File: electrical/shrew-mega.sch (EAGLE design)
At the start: 18 parts, among them IC1 Vreg +3V3, U1 DRV8231DSGR, U2 DRV8231DSGR, X1 PIN-1X-BIG, X2 PIN-1X-BIG, X3 PIN-1X-BIG, X4 PIN-1X-BIG, X5 PIN-1X-1.5MMSQ, X6 PIN-1X-1.5MMSQ

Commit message: rx mfg file trial run
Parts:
- added C10, C9: (no value), shrew-common:CAP0402-CAP
- added C8: (no value), shrew-common:CAP0805
- C6, C7: device shrew-common:CAP0402-CAP -> shrew-common:CAP0805
- IC1: value Vreg +3V3 -> (none); device shrew-common:V_REG_SOT89-SOT89 -> shrew-common:V_REG_LM1117SOT223
- U1, U2: value DRV8231DSGR -> DRV8244SQRYJRQ1; device shrew-core:DRV8231DSGR -> shrew-core:DRV8244SQRYJRQ1
- X5, X6: value PIN-1X-1.5MMSQ -> PIN-1X-BIG; device shrew-core:PIN-1X-1.5MMSQ -> shrew-core:PIN-1X-BIG
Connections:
- net +24V: now also C5.1, C6.1, C7.1
- net 3.3V: now also C8.1, IC1.OUT, IC1.OUT@1, U1.SLEEP_N, U2.SLEEP_N; no longer C5.1, IC1.VO, U1.VREF, U2.VREF
- net GND: now also C6.2, C7.2, C8.2, IC1.ADJ, U1.DIAG, U1.DRVOFF, U1.IPROPI, U1.ITRIP, U1.SR, U2.DIAG, U2.DRVOFF, U2.IPROPI, U2.ITRIP, U2.SR; no longer IC1.GND, IC1.TAB, U1.EPAD, U1.ISEN, U2.EPAD, U2.ISEN
- net N$10: now also C10.1, U2.OUT1, U2.OUT1_2; no longer C7.1, U1.OUT2
- net N$4: now also C9.2, U1.OUT2, U1.OUT2_2; no longer C6.2, U2.OUT1
- net N$5: now also C9.1, U1.OUT1, U1.OUT1_2; no longer C6.1, U2.OUT2
- net N$8: now also C10.2, U2.OUT2, U2.OUT2_2; no longer C7.2, U1.OUT1
- net SIG1: now also U2.EN_IN1; no longer U1.IN2
- net SIG2: now also U2.PH_IN2; no longer U1.IN1
- net SIG3: now also U1.EN_IN1; no longer U2.IN2
- net SIG4: now also U1.PH_IN2; no longer U2.IN1
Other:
- note added: "Current regulation disabled, OCP still used"
- note added: "Default slew rate 22V/us"
- note added: "Faults cause retry automatically"
- note added: "PWM mode"
- moved on the sheet: C1, C2, C3, C4, C5, C6, C7, JP1, R1

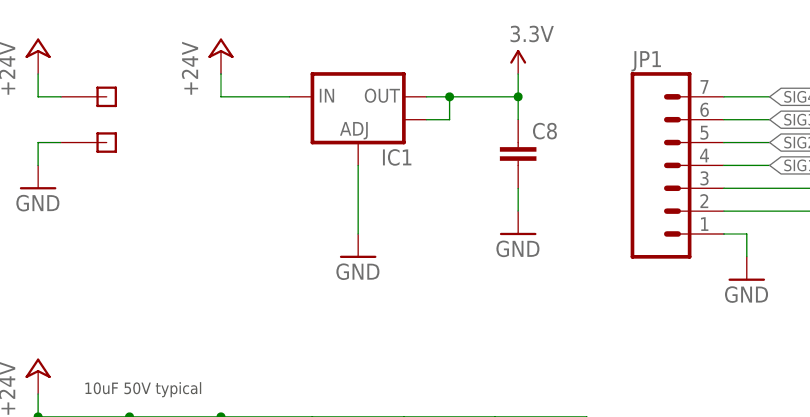
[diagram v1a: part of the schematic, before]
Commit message: changed v-reg on the mega variant to be more avail
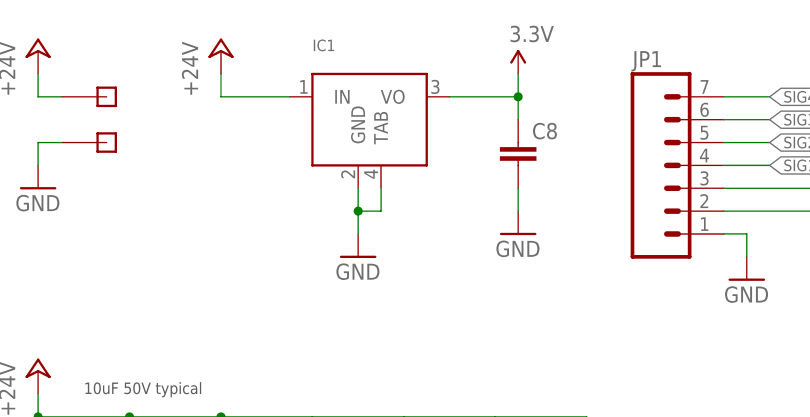
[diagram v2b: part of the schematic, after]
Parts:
- IC1: device shrew-common:V_REG_LM1117SOT223 -> shrew-common:V_REG_SOT-SOT223
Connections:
- net 3.3V: now also IC1.VO; no longer IC1.OUT, IC1.OUT@1
- net GND: now also IC1.GND, IC1.TAB; no longer IC1.ADJ

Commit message: schematic stitcher
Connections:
- net N$10 renamed MOTOR3
- net N$4 renamed MOTOR2
- net N$5 renamed MOTOR1
- net N$7 renamed V-ADC
- net N$8 renamed MOTOR4
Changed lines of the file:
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@@
 <wire x1="43.18" y1="58.42" x2="53.34" y2="58.42" width="0.1524" layer="91"/>
 <wire x1="53.34" y1="58.42" x2="53.34" y2="60.96" width="0.1524" layer="91"/>
+<junction x="43.18" y="58.42"/>
+<junction x="33.02" y="58.42"/>
+<junction x="22.86" y="58.42"/>
 </segment>
 <segment>
@@
 <wire x1="43.18" y1="71.12" x2="53.34" y2="71.12" width="0.1524" layer="91"/>
 <wire x1="53.34" y1="71.12" x2="53.34" y2="68.58" width="0.1524" layer="91"/>
+<junction x="22.86" y="71.12"/>
+<junction x="33.02" y="71.12"/>
+<junction x="43.18" y="71.12"/>
 </segment>
 <segment>
@@
 </segment>
 </net>
-<net name="N$4" class="0">
+<net name="MOTOR2" class="0">
 <segment>
 <pinref part="X1" gate="G$1" pin="P$1"/>
@@
 </segment>
 </net>
-<net name="N$5" class="0">
+<net name="MOTOR1" class="0">
 <segment>
 <pinref part="X2" gate="G$1" pin="P$1"/>
@@
 </segment>
 </net>
-<net name="N$8" class="0">
+<net name="MOTOR4" class="0">
 <segment>
 <pinref part="X3" gate="G$1" pin="P$1"/>
@@
 <pinref part="U2" gate="A" pin="OUT2"/>
 <wire x1="48.26" y1="-35.56" x2="50.8" y2="-35.56" width="0.1524" layer="91"/>
-</segment>
-</net>
-<net name="N$10" class="0">
+<junction x="50.8" y="-35.56"/>
+</segment>
+</net>
+<net name="MOTOR3" class="0">
 <segment>
 <pinref part="X4" gate="G$1" pin="P$1"/>
@@
 <wire x1="48.26" y1="-27.94" x2="50.8" y2="-27.94" width="0.1524" layer="91"/>
 <wire x1="50.8" y1="-27.94" x2="50.8" y2="-25.4" width="0.1524" layer="91"/>
+<junction x="50.8" y="-25.4"/>
 </segment>
 </net>
@@
 </segment>
 </net>
-<net name="N$7" class="0">
+<net name="V-ADC" class="0">
 <segment>
 <pinref part="JP1" gate="G$1" pin="3"/>

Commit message: initial work on integrated versions
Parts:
- added C11: (no value), shrew-common:CAP0805
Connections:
- new net SLEEP: U1.SLEEP_N, U2.SLEEP_N
- net +24V: now also C11.1
- net 3.3V: no longer U1.SLEEP_N, U2.SLEEP_N
- net GND: now also C11.2
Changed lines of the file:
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@@
 <layer number="97" name="Info" color="7" fill="1" visible="yes" active="yes"/>
 <layer number="98" name="Guide" color="6" fill="1" visible="yes" active="yes"/>
+<layer number="99" name="SpiceOrder" color="5" fill="1" visible="no" active="no"/>
 <layer number="100" name="Muster" color="7" fill="1" visible="no" active="no"/>
 <layer number="101" name="Patch_Top" color="12" fill="4" visible="no" active="yes"/>
@@
 <part name="P+11" library="shrew-common" deviceset="+24V" device=""/>
 <part name="P+12" library="shrew-common" deviceset="+24V" device=""/>
-<part name="P+13" library="shrew-common" deviceset="3.3V" device=""/>
 <part name="GND18" library="shrew-common" deviceset="GND" device=""/>
 <part name="X6" library="shrew-core" deviceset="PIN-1X" device="-BIG" value="PIN-1X-BIG"/>
@@
 <part name="JP1" library="shrew-common" deviceset="M07" device="-2MM-TH"/>
 <part name="GND1" library="shrew-common" deviceset="GND" device=""/>
-<part name="P+1" library="shrew-common" deviceset="3.3V" device=""/>
 <part name="R1" library="shrew-common" deviceset="RESISTOR" device="0402-RES"/>
 <part name="P+2" library="shrew-common" deviceset="+24V" device=""/>
@@
 <part name="P+3" library="shrew-common" deviceset="+24V" device=""/>
 <part name="P+4" library="shrew-common" deviceset="+24V" device=""/>
-<part name="P+5" library="shrew-common" deviceset="3.3V" device=""/>
-<part name="P+6" library="shrew-common" deviceset="3.3V" device=""/>
 <part name="GND4" library="shrew-common" deviceset="GND" device=""/>
 <part name="GND5" library="shrew-common" deviceset="GND" device=""/>
@@
 <part name="C7" library="shrew-common" deviceset="CAP" device="0805"/>
 <part name="IC1" library="shrew-common" deviceset="V_REG_SOT" device="-SOT223"/>
+<part name="P+1" library="shrew-common" deviceset="3.3V" device=""/>
+<part name="P+5" library="shrew-common" deviceset="3.3V" device=""/>
+<part name="C11" library="shrew-common" deviceset="CAP" device="0805"/>
+<part name="GND6" library="shrew-common" deviceset="GND" device=""/>
+<part name="P+6" library="shrew-common" deviceset="+24V" device=""/>
 </parts>
 <sheets>
@@
 <instance part="P+11" gate="1" x="-7.62" y="111.76"/>
 <instance part="P+12" gate="1" x="12.7" y="111.76"/>
-<instance part="P+13" gate="G$1" x="45.72" y="109.22"/>
 <instance part="GND18" gate="1" x="27.94" y="88.9"/>
 <instance part="X6" gate="G$1" x="0" y="101.6"/>
@@
 <instance part="JP1" gate="G$1" x="63.5" y="96.52"/>
 <instance part="GND1" gate="1" x="71.12" y="86.36"/>
-<instance part="P+1" gate="G$1" x="96.52" y="88.9"/>
 <instance part="R1" gate="G$1" x="86.36" y="96.52"/>
 <instance part="P+2" gate="1" x="104.14" y="104.14"/>
@@
 <instance part="P+3" gate="1" x="-5.08" y="38.1"/>
 <instance part="P+4" gate="1" x="-2.54" y="-20.32"/>
-<instance part="P+5" gate="G$1" x="-20.32" y="-35.56"/>
-<instance part="P+6" gate="G$1" x="-20.32" y="22.86"/>
 <instance part="GND4" gate="1" x="2.54" y="-66.04"/>
 <instance part="GND5" gate="1" x="2.54" y="-7.62"/>
@@
 <instance part="C7" gate="G$1" x="53.34" y="63.5"/>
 <instance part="IC1" gate="G$1" x="27.94" y="106.68"/>
+<instance part="P+1" gate="G$1" x="45.72" y="109.22"/>
+<instance part="P+5" gate="G$1" x="111.76" y="96.52"/>
+<instance part="C11" gate="G$1" x="81.28" y="68.58"/>
+<instance part="GND6" gate="1" x="81.28" y="60.96"/>
+<instance part="P+6" gate="1" x="81.28" y="78.74"/>
 </instances>
 <busses>
@@
 <label x="50.8" y="-48.26" size="1.27" layer="95" xref="yes"/>
 </segment>
-</net>
-<net name="3.3V" class="0">
-<segment>
-<pinref part="C8" gate="G$1" pin="1"/>
-<pinref part="P+13" gate="G$1" pin="3.3V"/>
-<wire x1="45.72" y1="109.22" x2="45.72" y2="106.68" width="0.1524" layer="91"/>
-<pinref part="IC1" gate="G$1" pin="VO"/>
-<wire x1="45.72" y1="106.68" x2="45.72" y2="104.14" width="0.1524" layer="91"/>
-<wire x1="38.1" y1="106.68" x2="45.72" y2="106.68" width="0.1524" layer="91"/>
-<junction x="45.72" y="106.68"/>
-</segment>
-<segment>
-<pinref part="JP1" gate="G$1" pin="2"/>
-<pinref part="P+1" gate="G$1" pin="3.3V"/>
-<wire x1="68.58" y1="93.98" x2="78.74" y2="93.98" width="0.1524" layer="91"/>
-<wire x1="78.74" y1="93.98" x2="78.74" y2="86.36" width="0.1524" layer="91"/>
-<wire x1="78.74" y1="86.36" x2="96.52" y2="86.36" width="0.1524" layer="91"/>
-<wire x1="96.52" y1="86.36" x2="96.52" y2="88.9" width="0.1524" layer="91"/>
-</segment>
+<segment>
+<pinref part="C11" gate="G$1" pin="2"/>
+<pinref part="GND6" gate="1" pin="GND"/>
+<wire x1="81.28" y1="66.04" x2="81.28" y2="63.5" width="0.1524" layer="91"/>
+</segment>
+</net>
+<net name="SLEEP" class="0">
 <segment>
 <pinref part="U1" gate="A" pin="SLEEP_N"/>
-<pinref part="P+6" gate="G$1" pin="3.3V"/>
-<wire x1="5.08" y1="20.32" x2="-20.32" y2="20.32" width="0.1524" layer="91"/>
-<wire x1="-20.32" y1="20.32" x2="-20.32" y2="22.86" width="0.1524" layer="91"/>
+<wire x1="5.08" y1="20.32" x2="2.54" y2="20.32" width="0.1524" layer="91"/>
+<label x="2.54" y="20.32" size="1.27" layer="95" rot="R180" xref="yes"/>
 </segment>
 <segment>
 <pinref part="U2" gate="A" pin="SLEEP_N"/>
-<pinref part="P+5" gate="G$1" pin="3.3V"/>
-<wire x1="5.08" y1="-38.1" x2="-20.32" y2="-38.1" width="0.1524" layer="91"/>
-<wire x1="-20.32" y1="-38.1" x2="-20.32" y2="-35.56" width="0.1524" layer="91"/>
+<wire x1="5.08" y1="-38.1" x2="2.54" y2="-38.1" width="0.1524" layer="91"/>
+<label x="2.54" y="-38.1" size="1.27" layer="95" rot="R180" xref="yes"/>
 </segment>
 </net>
@@
 <wire x1="-5.08" y1="33.02" x2="-5.08" y2="35.56" width="0.1524" layer="91"/>
 </segment>
+<segment>
+<pinref part="C11" gate="G$1" pin="1"/>
+<pinref part="P+6" gate="1" pin="+24V"/>
+<wire x1="81.28" y1="73.66" x2="81.28" y2="76.2" width="0.1524" layer="91"/>
+</segment>
 </net>
 <net name="MOTOR2" class="0">
@@
 </segment>
 </net>
+<net name="3.3V" class="0">
+<segment>
+<pinref part="P+5" gate="G$1" pin="3.3V"/>
+<wire x1="111.76" y1="96.52" x2="111.76" y2="93.98" width="0.1524" layer="91"/>
+<pinref part="JP1" gate="G$1" pin="2"/>
+<wire x1="111.76" y1="93.98" x2="68.58" y2="93.98" width="0.1524" layer="91"/>
+</segment>
+<segment>
+<pinref part="IC1" gate="G$1" pin="VO"/>
+<pinref part="P+1" gate="G$1" pin="3.3V"/>
+<wire x1="38.1" y1="106.68" x2="45.72" y2="106.68" width="0.1524" layer="91"/>
+<wire x1="45.72" y1="106.68" x2="45.72" y2="109.22" width="0.1524" layer="91"/>
+<pinref part="C8" gate="G$1" pin="1"/>
+<wire x1="45.72" y1="104.14" x2="45.72" y2="106.68" width="0.1524" layer="91"/>
+<junction x="45.72" y="106.68"/>
+</segment>
+</net>

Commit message: up-rev
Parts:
- removed JP1: (no value), shrew-common:M07-2MM-TH
- added ANT1, ANT2: 74889302450, shrew-common:ANTENNA2SMD
- added C12: DNP, shrew-common:CAP0402-CAP
- added C13, C17: 470n, shrew-common:CAP0402-REV
- added C14, C15: (no value), shrew-common:CAP0402-CAP
- added C16, C18, C19, C20, C21, C22, C23: (no value), shrew-common:CAP0805
- added C24, C25, C27: 10u, shrew-common:CAP0805
- added C26: 100n, shrew-common:CAP0402-REV
- added D1: 3V6, shrew-common:DIODE-ZENER-BZT52
- added D2: (no value), shrew-common:DIODESOD
- added EDGE1: (no value), shrew-common:M05PTH
- added FL1: 2450FM07D0034T, shrew-core:2450FM07D0034T
- added L1: 15u, shrew-common:INDUCTOR0805
- added L2: 6u8, shrew-common:INDUCTOR0805
- added LED1: SK6812-EC20, shrew-core:SK6812-EC20
- added R2, R3: 10K, shrew-common:RESISTOR0402-REV
- added R4: (no value), shrew-common:RESISTOR0402-RES
- added U3, U4: DRV8244SQRYJRQ1, shrew-core:DRV8244SQRYJRQ1
- added Y1: 52MHz TCXO, shrew-common:OSCILLATOR-TG2016SMN
- C1: value (none) -> 1n; device shrew-common:CAP0805 -> shrew-common:CAP0402-REV
- C10, C9: value (none) -> 100n; device shrew-common:CAP0402-CAP -> shrew-common:CAP0402-REV
- C11: value (none) -> 10uF 25V
- C2: value (none) -> 470n; device shrew-common:CAP0805 -> shrew-common:CAP0402-REV
- C3, C4: value (none) -> 10n; device shrew-common:CAP0805 -> shrew-common:CAP0402-REV
- C5, C6, C7, C8: value (none) -> 100n; device shrew-common:CAP0805 -> shrew-common:CAP0402-REV
- IC1: value (none) -> LMR16006YQ3DDCTQ1; device shrew-common:V_REG_SOT-SOT223 -> shrew-core:LMR16006XDDCR
- R1: value (none) -> 10K; device shrew-common:RESISTOR0402-RES -> shrew-common:RESISTOR0402-REV
- U1: value DRV8244SQRYJRQ1 -> ESP32-PICO-D4; device shrew-core:DRV8244SQRYJRQ1 -> shrew-core:ESP32-PICO-D4
- U2: value DRV8244SQRYJRQ1 -> SX1280IMLTRT; device shrew-core:DRV8244SQRYJRQ1 -> shrew-core:SX1280IMLTRT
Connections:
- removed net SLEEP: U1.SLEEP_N, U2.SLEEP_N
- new net AUX1: EDGE1.1, U1.IO19
- new net AUX2: EDGE1.2, U1.IO22
- new net BATT-ADC: C17.1, D1.C, R2.2, R3.1, U1.IO4
- new net ESP-BOOT: C12.2, U1.IO0(BOOT)
- new net ESP-EN: C13.2, R1.1, U1.EN
- new net N$1: ANT1.SIGNAL, U1.LNA_IN
- new net N$10: C26.1, D2.C, IC1.SW, L2.1
- new net N$11: C3.2, U2.VR_PA
- new net N$2: C1.1, Y1.OUT
- new net N$3: C1.2, U2.XTA
- new net N$4: C26.2, IC1.CB
- new net N$5: U1.IO14
- new net N$6: FL1.IN, U2.RFIO
- new net N$7: ANT2.SIGNAL, FL1.OUT
- new net N$8: U1.IO2
- new net N$9: L1.2, U2.DCC_SW
- new net RADIO-BUSY: U1.IO23, U2.BUSY
- new net RADIO-CS: U1.IO32, U2.NSS_CTS
- new net RADIO-DIO: U1.IO18, U2.DIO1
- new net RADIO-RST: U1.IO21, U2.NRESET, U3.SLEEP_N, U4.SLEEP_N
- new net RADIO-VDD: C2.2, C4.2, L1.1, U2.DCC_FB, U2.VDD_INN
- new net RGBLED: LED1.DIN, U1.IO5
- new net SPI-MISO: U1.IO26, U2.MISO_TX
- new net SPI-MOSI: U1.IO25, U2.MOSI_RX
- new net SPI-SCK: U1.IO33, U2.SCK_RTSN
- new net U0RXD: EDGE1.3, U1.U0RXD(IO3)
- new net U0TXD: EDGE1.4, U1.U0TXD(IO1)
- net +24V: now also C16.1, C18.1, C19.1, C20.1, C21.1, C22.1, C23.1, C24.1, IC1.SHDN, IC1.VIN, R4.2, U3.VM, U4.VM; no longer C1.1, C11.1, C2.1, C3.1, C4.1, C5.1, C6.1, C7.1, IC1.IN, R1.2, U1.VM, U2.VM
- net 3.3V: now also C10.1, C11.1, C25.1, C27.1, C5.2, C6.2, C7.2, C9.1, IC1.FB, L2.2, LED1.VDD, R1.2, U1.VDD3P3_CPU, U1.VDD3P3_RTC, U1.VDDA, U1.VDDA3P3, U1.VDD_SDIO, U2.VBAT, U2.VBAT_IO, Y1.VCC; no longer IC1.VO, JP1.2
- net GND: now also C10.2, C12.1, C13.1, C16.2, C17.2, C18.2, C19.2, C2.1, C20.2, C21.2, C22.2, C23.2, C24.2, C25.2, C27.2, C3.1, C4.1, C5.1, C6.1, C7.1, C9.2, D1.A, D2.A, EDGE1.5, LED1.VSS(GND), R2.1, U1.IO15/MTDO, U2.GND_2, U2.GND_3, U2.GND_4, U2.GND_5, U2.GND_6, U2.GND_7, U3.DIAG, U3.DRVOFF, U3.GND, U3.IPROPI, U3.ITRIP, U3.SR, U4.DIAG, U4.DRVOFF, U4.GND, U4.IPROPI, U4.ITRIP, U4.SR, Y1.GND; no longer C1.2, C2.2, C3.2, C4.2, C5.2, C6.2, C7.2, IC1.TAB, JP1.1, U1.DIAG, U1.DRVOFF, U1.IPROPI, U1.ITRIP, U1.SR, U2.DIAG, U2.DRVOFF, U2.IPROPI, U2.ITRIP, U2.SR
- net MOTOR1: now also C14.1, U3.OUT1, U3.OUT1_2; no longer C9.1, U1.OUT1, U1.OUT1_2
- net MOTOR2: now also C14.2, U3.OUT2, U3.OUT2_2; no longer C9.2, U1.OUT2, U1.OUT2_2
- net MOTOR3: now also C15.1, U4.OUT1, U4.OUT1_2; no longer C10.1, U2.OUT1, U2.OUT1_2
- net MOTOR4: now also C15.2, U4.OUT2, U4.OUT2_2; no longer C10.2, U2.OUT2, U2.OUT2_2
- net SIG1: now also U1.IO13, U4.EN_IN1; no longer JP1.4, U2.EN_IN1
- net SIG2: now also U1.IO27, U4.PH_IN2; no longer JP1.5, U2.PH_IN2
- net SIG3: now also U1.SD2/IO9, U3.EN_IN1; no longer JP1.6, U1.EN_IN1
- net SIG4: now also U1.SD3/IO10, U3.PH_IN2; no longer JP1.7, U1.PH_IN2
- net V-ADC: now also R3.2, R4.1; no longer JP1.3, R1.1
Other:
- note added: "LOW = Quiet Boot"
- note added: "actually only for tweezers to squeeze"
- note added: "not actually +24V"
- moved on the sheet: C1, C10, C11, C2, C3, C4, C5, C6, C7, C8, C9, R1

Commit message: second gen gerbers
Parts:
- R4: device shrew-common:RESISTOR0402-RES -> shrew-common:RESISTOR0402-REV
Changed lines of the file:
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@@
 <part name="C25" library="shrew-common" deviceset="CAP" device="0805" value="10u"/>
 <part name="GND23" library="shrew-common" deviceset="GND" device=""/>
-<part name="R4" library="shrew-common" deviceset="RESISTOR" device="0402-RES"/>
+<part name="R4" library="shrew-common" deviceset="RESISTOR" device="0402-REV"/>
 <part name="P+10" library="shrew-common" deviceset="+24V" device=""/>
 <part name="U3" library="shrew-core" deviceset="DRV8244SQRYJRQ1" device=""/>
